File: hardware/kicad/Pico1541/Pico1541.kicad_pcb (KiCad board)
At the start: 2 copper layers, 100 x 76 mm, 45 parts, among them J1 SWD, J2 Serial, J3 Display/Keys, J4 Micro SD Card, J5 5V_EXT, J6 USB_A, J7 OLED/Key_Hat, J8 OLED, J9 DIN-6, Q1 MMBT3904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

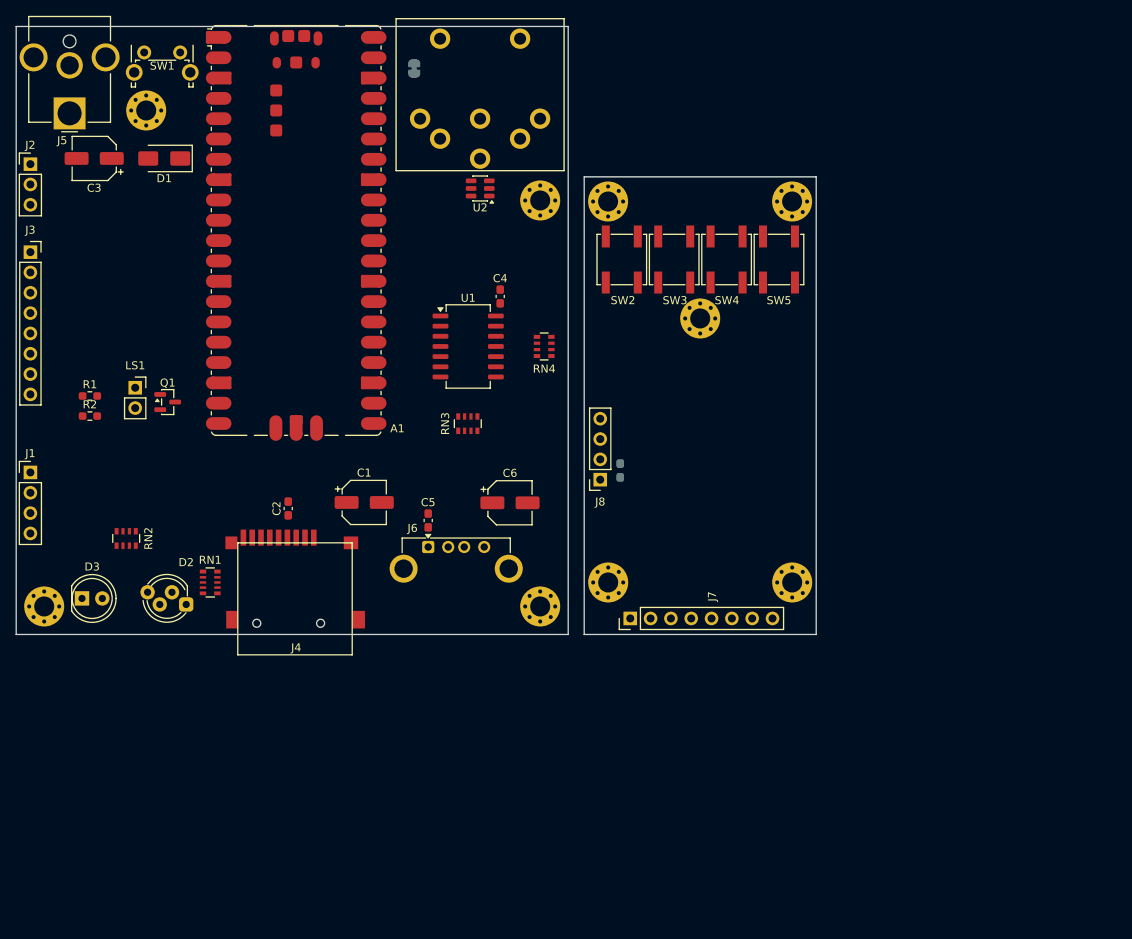
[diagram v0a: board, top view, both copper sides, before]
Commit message: Completed PCB design. Still missing break-off tabs.
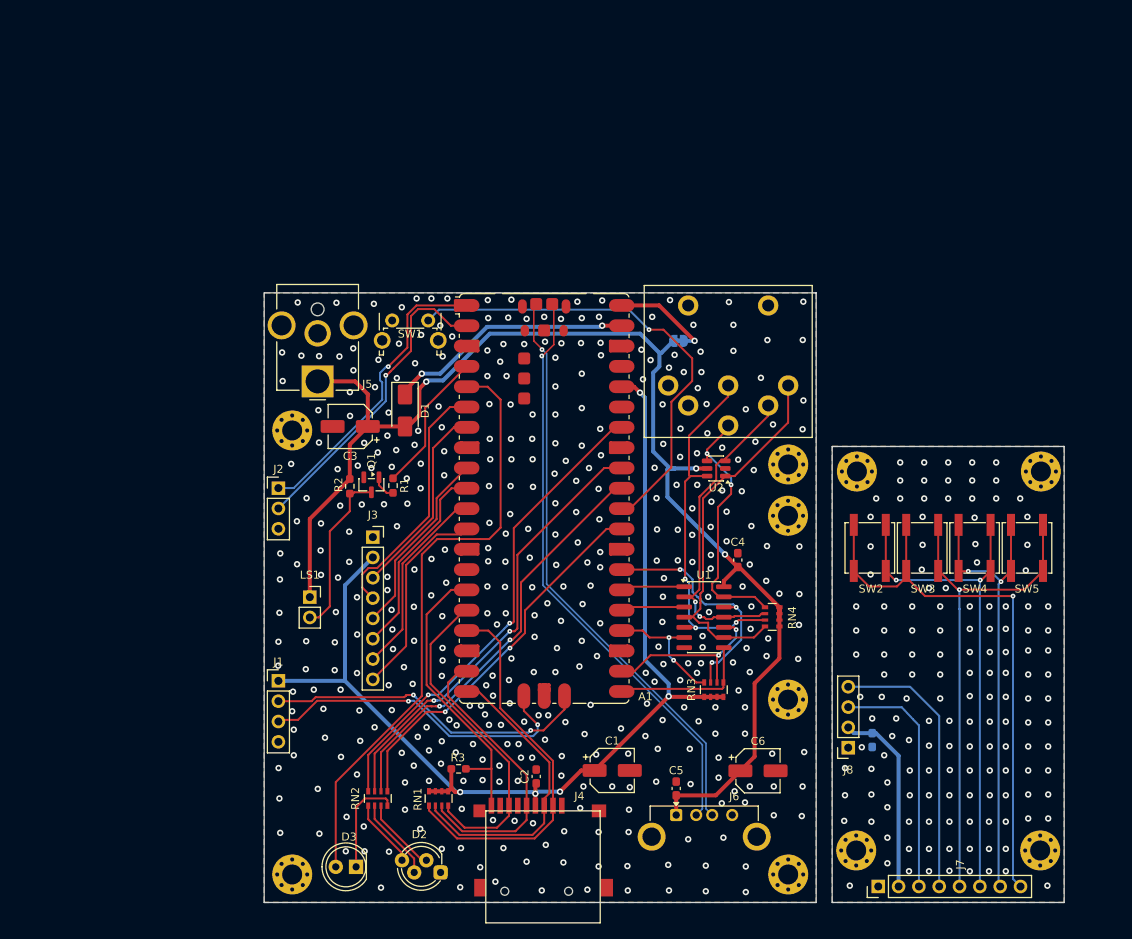
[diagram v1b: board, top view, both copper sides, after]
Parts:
- removed REF** (x9): MountingHole_2.5mm_Pad_Via, MountingHole:MountingHole_2.5mm_Pad_Via
- added H1: M, MountingHole:MountingHole_2.5mm_Pad_Via, F.Cu at (96.0, 81.0)
- added H10: M, MountingHole:MountingHole_2.5mm_Pad_Via, F.Cu at (189.6, 86.1)
- added H2: M, MountingHole:MountingHole_2.5mm_Pad_Via, F.Cu at (96.0, 136.5)
- added H3: M, MountingHole:MountingHole_2.5mm_Pad_Via, F.Cu at (158.0, 136.5)
- added H4: M, MountingHole:MountingHole_2.5mm_Pad_Via, F.Cu at (158.0, 114.6)
- added H5: M, MountingHole:MountingHole_2.5mm_Pad_Via, F.Cu at (158.0, 91.7)
- added H6: M, MountingHole:MountingHole_2.5mm_Pad_Via, F.Cu at (158.0, 85.2)
- added H7: M, MountingHole:MountingHole_2.5mm_Pad_Via, F.Cu at (166.5, 133.5)
- added H8: M, MountingHole:MountingHole_2.5mm_Pad_Via, F.Cu at (189.5, 133.5)
- added H9: M, MountingHole:MountingHole_2.5mm_Pad_Via, F.Cu at (166.6, 86.1)
- added R3: 10K, Resistor_SMD:R_0603_1608Metric_Pad0.98x0.95mm_HandSolder, F.Cu at (116.8, 123.3)
- D3: value LED_PWR -> PWR_STATE
- RN1: footprint Resistor_SMD:R_Array_Convex_5x0603 -> Resistor_SMD:R_Array_Convex_4x0603
- U1: footprint Package_SO:SO-14_5.3x10.2mm_P1.27mm -> Package_SO:SO-14_3.9x8.65mm_P1.27mm
- moved J3 55.7 mm to (106.1, 94.3)
- moved J2 51.0 mm to (94.3, 88.2)
- moved D3 47.9 mm to (104.0, 135.5), turned to 180 degrees
- moved SW2 47.5 mm to (168.2, 95.7)
- moved SW3 47.5 mm to (174.8, 95.7)
- moved SW4 47.5 mm to (181.3, 95.7)
- moved SW5 47.5 mm to (187.8, 95.7)
- moved JP1 47.5 mm to (144.3, 69.8), turned to 0 degrees
- moved C3 46.3 mm to (103.2, 80.5)
- moved D2 46.2 mm to (114.5, 136.2)
- moved C7 46.1 mm to (168.5, 119.7), turned to -90 degrees
- moved U2 45.8 mm to (149.0, 85.8)
- moved A1 45.6 mm to (127.5, 89.5)
- moved C1 45.6 mm to (136.0, 123.5)
- moved C2 45.6 mm to (126.5, 124.2)
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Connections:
- net Net-(A1-USB_DM) renamed /USB_DN
- net Net-(A1-USB_DP) renamed /USB_DP
- net Net-(A1-VSYS) renamed VS
- A1 pad 29: unconnected-(A1-GPIO22-Pad29) -> Net-(A1-GPIO22)
- A1 pad 5: unconnected-(A1-GPIO3-Pad5) -> /PLED_N
- C7 pad 1: Net-(J7-Pin_1) -> +3.3VA
- C7 pad 2: Net-(J7-Pin_2) -> GNDA
- D3 pad 1: GND -> Net-(D3-KA)
- D3 pad 2: Net-(D3-A) -> /PLED_N
- J7 pad 1: Net-(J7-Pin_1) -> GNDA
- J7 pad 2: Net-(J7-Pin_2) -> +3.3VA
- J8 pad 1: Net-(J7-Pin_1) -> GNDA
- J8 pad 2: Net-(J7-Pin_2) -> +3.3VA
- RN1 pad 5: +3.3V -> /SD_CD
- RN1 pad 6: /SD_CD -> /SD_CMD
- RN1 pad 7: /SD_CMD -> /SD_CLK
- RN1 pad 8: /SD_CLK -> /SD_DAT0
- RN2 pad 1: Net-(A1-GPIO26_ADC0) -> Net-(A1-GPIO22)
- RN2 pad 2: Net-(A1-GPIO27_ADC1) -> Net-(A1-GPIO26_ADC0)
- RN2 pad 3: Net-(A1-GPIO28_ADC2) -> Net-(A1-GPIO27_ADC1)
- RN2 pad 4: +3.3V -> Net-(A1-GPIO28_ADC2)
- RN2 pad 5: Net-(D3-A) -> Net-(D2-BA)
- RN2 pad 6: Net-(D2-BA) -> Net-(D2-GA)
- RN2 pad 7: Net-(D2-GA) -> Net-(D2-RA)
- RN2 pad 8: Net-(D2-RA) -> Net-(D3-KA)
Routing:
- net +5V: track 0.00 -> 166.2 mm, vias 0 -> 3
- net +3.3V: track 0.00 -> 134.9 mm, vias 0 -> 5
- net /PLED_N: track 0.00 -> 75.6 mm
- net /USB_DN: track 0.00 -> 73.3 mm, vias 0 -> 1
- net /USB_DP: track 0.00 -> 73.3 mm, vias 0 -> 1
- net Net-(J7-Pin_8): track 0.00 -> 71.2 mm, vias 0 -> 1
- net Net-(J7-Pin_6): track 0.00 -> 63.9 mm, vias 0 -> 2
- net Net-(J7-Pin_5): track 0.00 -> 63.7 mm, vias 0 -> 1
- net Net-(A1-GPIO28_ADC2): track 0.00 -> 60.1 mm, vias 0 -> 2
- net Net-(A1-RUN): track 0.00 -> 59.1 mm, vias 0 -> 1
- net Net-(J7-Pin_7): track 0.00 -> 57.5 mm, vias 0 -> 2
- net Net-(A1-GPIO27_ADC1): track 0.00 -> 55.8 mm, vias 0 -> 2
- net Net-(A1-GPIO26_ADC0): track 0.00 -> 52.2 mm, vias 0 -> 2
- net /SD_CD: track 0.00 -> 48.2 mm
- net /DATA_IEC: track 0.00 -> 47.8 mm
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- added copper zone on B.Cu, net GND
- added copper zone on F.Cu, net GND
- added copper zone on B.Cu, net GNDA
- added copper zone on F.Cu, net GNDA
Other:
- board size 100 x 76 mm -> 100 x 76.2 mm

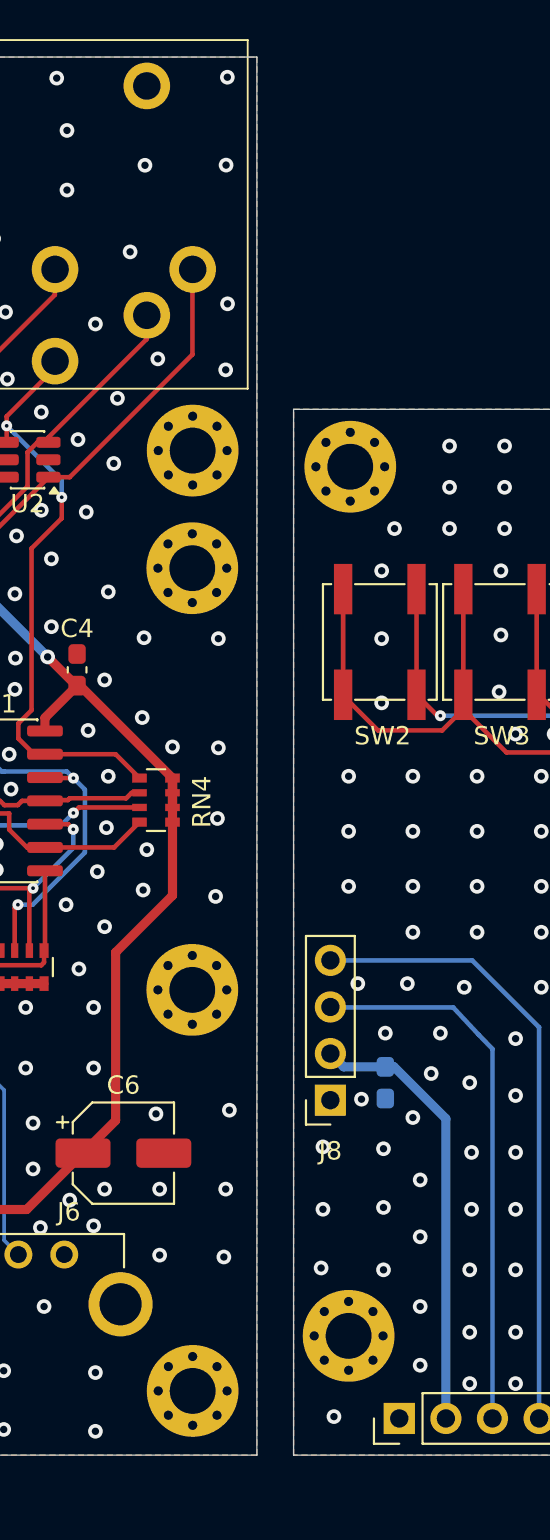
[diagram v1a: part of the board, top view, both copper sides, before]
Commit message: Added mouse bites to PCB parts.
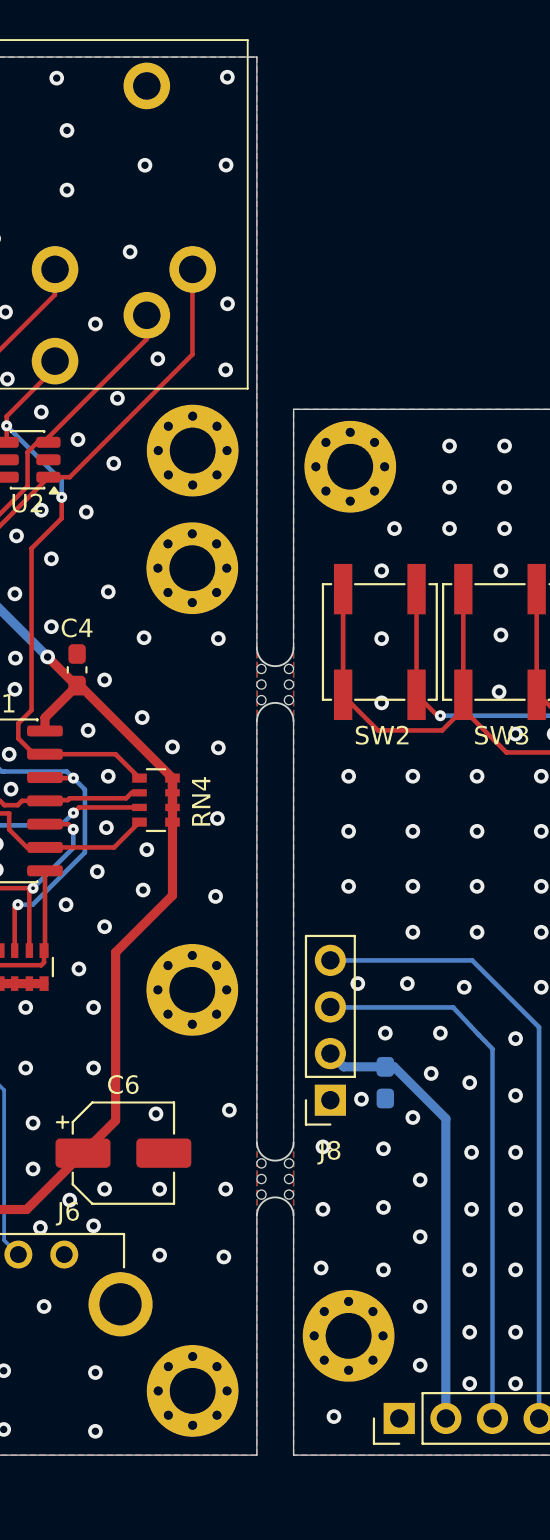
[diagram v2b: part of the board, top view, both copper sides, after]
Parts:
- added REF**: MouseBite-Slot_2.0x2.0mm_outset_D0.5mm_P0.85mm_3h, Panelization:MouseBite-Slot_2.0x2.0mm_outset_D0.5mm_P0.85mm_3h, F.Cu at (163.5, 98.0)
- added REF**: MouseBite-Slot_2.0x2.0mm_outset_D0.5mm_P0.85mm_3h, Panelization:MouseBite-Slot_2.0x2.0mm_outset_D0.5mm_P0.85mm_3h, F.Cu at (163.5, 125.0)
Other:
- outline, holes or cut-outs redrawn

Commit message: Finalized design.
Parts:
- added FID1: Fiducial, Fiducial:Fiducial_1mm_Mask3mm, F.Cu at (159.2, 98.5)
- added FID2: Fiducial, Fiducial:Fiducial_1mm_Mask3mm, B.Cu at (159.2, 98.5)
- added FID3: Fiducial, Fiducial:Fiducial_1mm_Mask3mm, B.Cu at (165.7, 104.5)
- added FID4: Fiducial, Fiducial:Fiducial_1mm_Mask3mm, F.Cu at (165.7, 104.5)
- added FID5: Fiducial, Fiducial:Fiducial_1mm_Mask3mm, F.Cu at (94.8, 131.4)
- added FID6: Fiducial, Fiducial:Fiducial_1mm_Mask3mm, B.Cu at (94.8, 131.4)
- added REF**: Symbol_CreativeCommons_SilkScreenTop_Type2_Big, Symbol:Symbol_CreativeCommons_SilkScreenTop_Type2_Big, F.Cu at (178.4, 109.3)
- added REF**: Symbol_CreativeCommons_SilkScreenTop_Type2_Big, Symbol:Symbol_CreativeCommons_SilkScreenTop_Type2_Big, B.Cu at (105.7, 126.0)
- added REF**: Symbol_CC-Noncommercial_CopperTop_Small, Symbol:Symbol_CC-Noncommercial_CopperTop_Small, B.Cu at (96.0, 126.2)
- added REF**: Symbol_CreativeCommons_SilkScreenTop_Type2_Big, Symbol:Symbol_CreativeCommons_SilkScreenTop_Type2_Big, F.Cu at (102.8, 119.7)
- added REF**: Symbol_CC-Noncommercial_CopperTop_Small, Symbol:Symbol_CC-Noncommercial_CopperTop_Small, F.Cu at (182.8, 87.0)
- added REF**: Symbol_CC-Noncommercial_CopperTop_Small, Symbol:Symbol_CC-Noncommercial_CopperTop_Small, F.Cu at (96.0, 126.2)
- added REF**: Symbol_CC-Noncommercial_CopperTop_Small, Symbol:Symbol_CC-Noncommercial_CopperTop_Small, B.Cu at (182.8, 87.0)
- added REF**: KiCad-Logo2_12mm_SilkScreen, Symbol:KiCad-Logo2_12mm_SilkScreen, B.Cu at (129.7, 115.0)
- added REF**: Symbol_CreativeCommons_SilkScreenTop_Type2_Big, Symbol:Symbol_CreativeCommons_SilkScreenTop_Type2_Big, B.Cu at (174.4, 89.2)
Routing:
- net GNDA: vias 143 -> 139
- net GND: vias 395 -> 398
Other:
- board text added: "Pico1541 - v1"

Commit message: Added Gerber files for final design for JLCPCB.
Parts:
- moved A1 12.5 mm to (134.0, 78.8)
- moved C1 12.5 mm to (142.5, 112.8)
- moved C2 12.5 mm to (133.0, 113.6)
- moved C3 12.5 mm to (109.8, 69.8)
- moved C4 12.5 mm to (158.2, 86.5)
- moved C5 12.5 mm to (150.5, 115.1)
- moved C6 12.5 mm to (160.7, 112.9)
- moved C7 12.5 mm to (175.0, 109.0)
- moved D1 12.5 mm to (116.6, 67.8)
- moved D2 12.5 mm to (121.0, 125.6)
- moved D3 12.5 mm to (110.5, 124.9)
- moved FID1 12.5 mm to (165.7, 87.8)
- moved FID2 12.5 mm to (165.7, 87.8)
- moved FID3 12.5 mm to (172.2, 93.8)
- moved FID4 12.5 mm to (172.2, 93.8)
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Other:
- outline, holes or cut-outs redrawn
